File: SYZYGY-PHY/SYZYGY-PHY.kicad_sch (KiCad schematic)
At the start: 43 parts, among them J1 QTH-020-01-X-D-DP-A, J2 ARJM11C7-502-KB-EW2, J3 Conn_01x10, U1 GPY111, U2 TXB0106RGY, U3 TXB0106RGY, Y1 Crystal_GND24

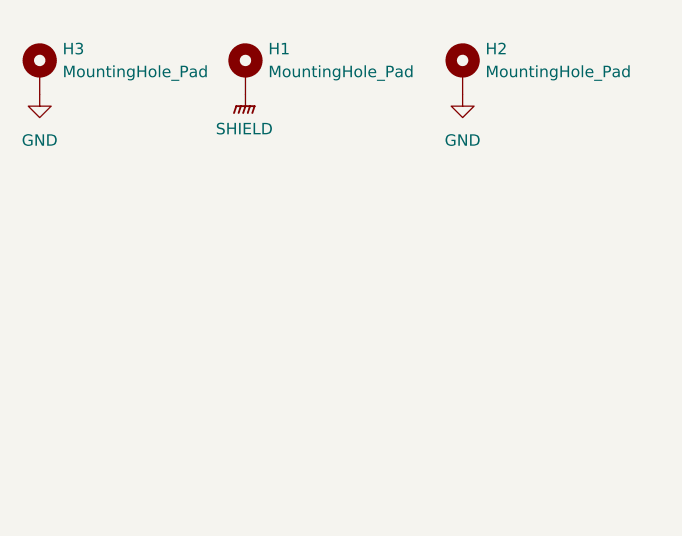
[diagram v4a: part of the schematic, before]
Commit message: adding power indicator LED
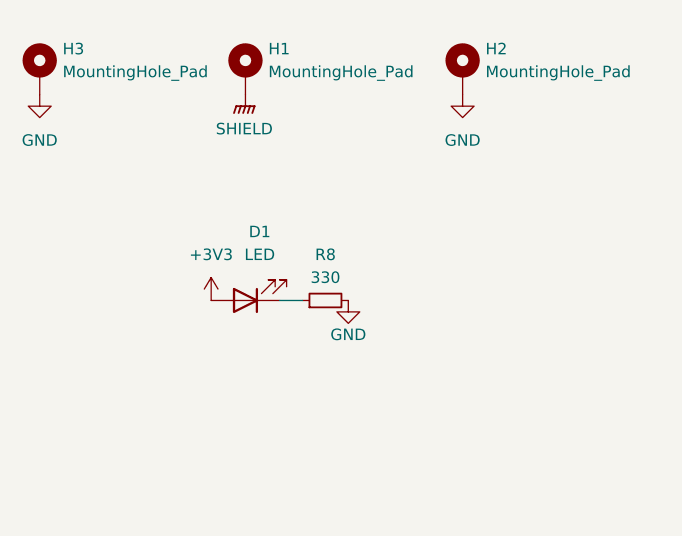
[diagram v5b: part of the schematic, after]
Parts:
- added D1: LED, LED_SMD:LED_0805_2012Metric, symbol Device:LED
- added R8: 330, Resistor_SMD:R_0805_2012Metric_Pad1.20x1.40mm_HandSolder, symbol Device:R_Small
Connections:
- net +3V3: now also D1.2 (A)
- net GND: now also R8.2
- new net: D1.1 (K), R8.1

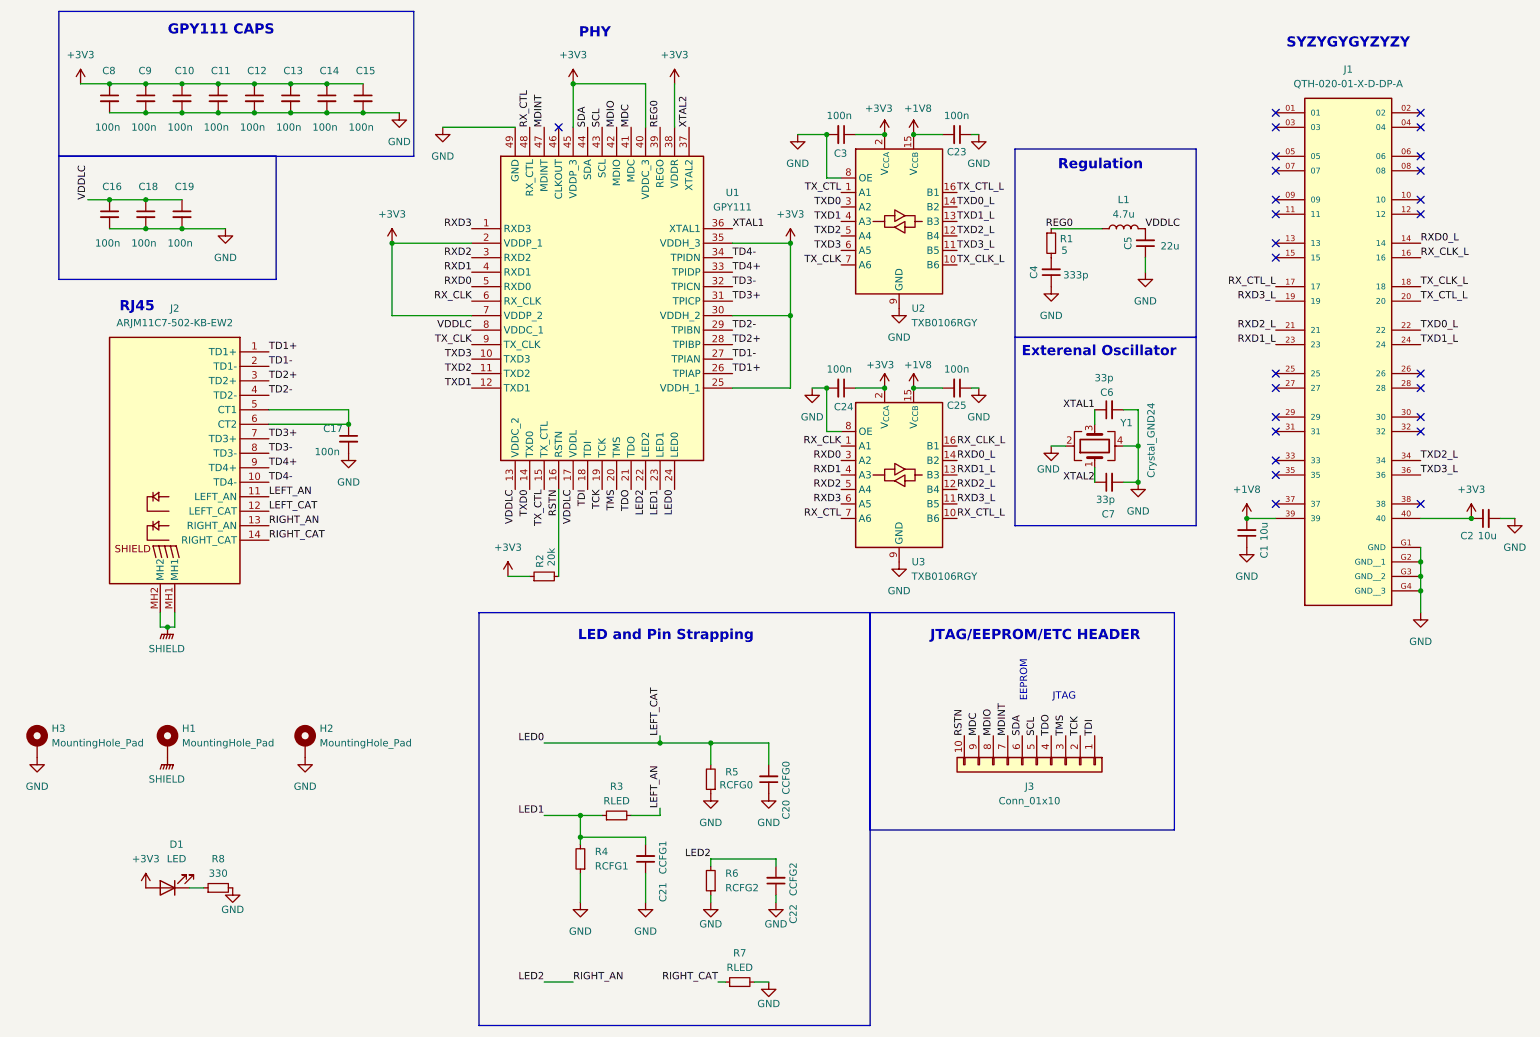
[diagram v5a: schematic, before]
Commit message: misc changes + SYZYGY-PHY fixes
fix up KiCad paths to be slightly friendlier to sharing between
machines; assert that we only want to use the library from `../`
relative so the 3d model path is valid.

SYZYGY-PHY fixes:
- add startup RC circuit to hold reset low for >1ms
- add calibration resistors between PHY C+/- and GND
- remove VDDLC from 3.3V net in schematic (not fully routed in PCB)
- update clock to a more frequency stable model, change CL caps accordingly
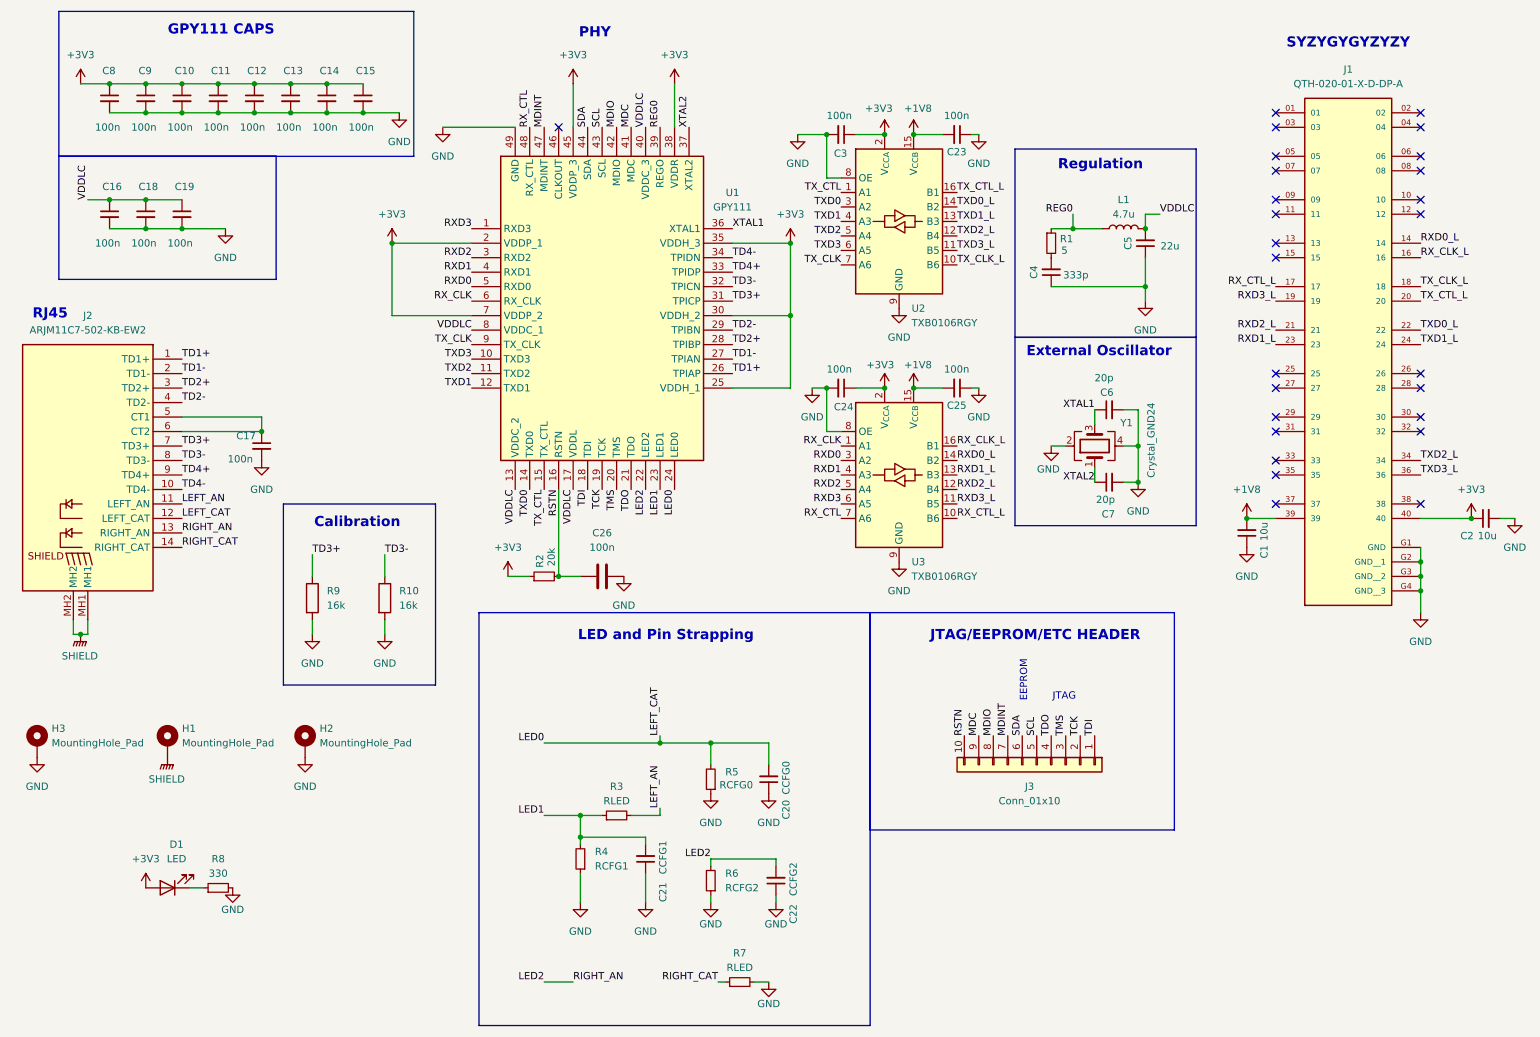
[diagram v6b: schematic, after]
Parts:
- added C26: 100n, Capacitor_SMD:C_0805_2012Metric_Pad1.18x1.45mm_HandSolder, symbol Device:C
- added R10, R9: 16k, Resistor_SMD:R_0805_2012Metric_Pad1.20x1.40mm_HandSolder, symbol Device:R
- C6, C7: value 33p -> 20p
- J2: App Note (none) -> https://ww1.microchip.com/downloads/en/Appnotes/VPPD-01740.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; Ref 2 (none) -> https://electronics.stackexchange.com/questions/637179/what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
- Y1: Manufacturer (none) -> TSX-3225 25.0000MF18X-G0; Mouser FA-238 25.0000MB-I -> 732-TSX-322MF18X-G
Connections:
- net +3V3: no longer U1.40 (VDDC_3)
- net GND: now also C26.1, R10.2, R9.2
- net RSTN: now also C26.2
- net TD3+: now also R9.1
- net TD3-: now also R10.1
- net VDDLC: now also U1.40 (VDDC_3)
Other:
- note added: "Calibration"
- note added: "External Oscillator"
- note removed: "Exterenal Oscillator"
- moved on the sheet: C17, J2

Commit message: adding inductor footprint for 2016 metric sized inductor, and changed L1 footprint and added to the pcb, updated the schematic with the new inductor part and datasheet link
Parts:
- L1: footprint Inductor_SMD:L_0805_2012Metric_Pad1.05x1.20mm_HandSolder -> local:Inductor 0806 (2016 metric); Part MLZ2012N4R7LT000 -> MAKK2016T4R7M
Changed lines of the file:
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@@
 			)
 		)
-		(property "Footprint" "Inductor_SMD:L_0805_2012Metric_Pad1.05x1.20mm_HandSolder"
+		(property "Footprint" "local:Inductor 0806 (2016 metric)"
 			(at 213.36 52.07 0)
 			(effects
@@
 			)
 		)
-		(property "Datasheet" "https://product.tdk.com/system/files/dam/doc/product/inductor/inductor/smd/catalog/inductor_commercial_decoupling_mlz2012_en.pdf"
+		(property "Datasheet" "https://www.mouser.com/datasheet/2/396/wound10_e-1396630.pdf"
 			(at 213.36 52.07 0)
 			(effects
@@
 			)
 		)
-		(property "Part" "MLZ2012N4R7LT000 "
+		(property "Part" "MAKK2016T4R7M"
 			(at 213.36 52.07 90)
 			(effects

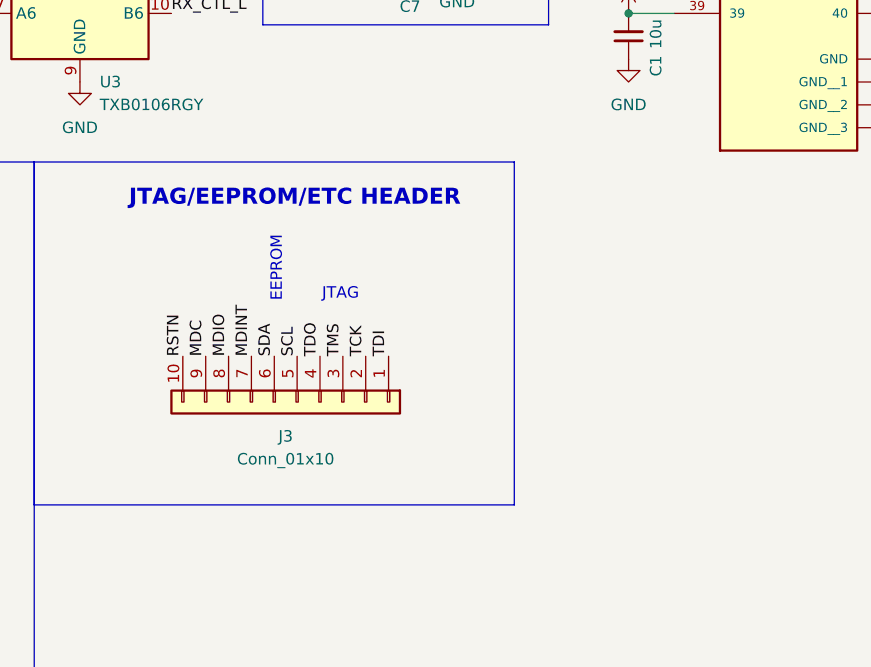
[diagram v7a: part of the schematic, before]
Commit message: adding a GND header, adding 3.3V and 1.8V 1x2 header
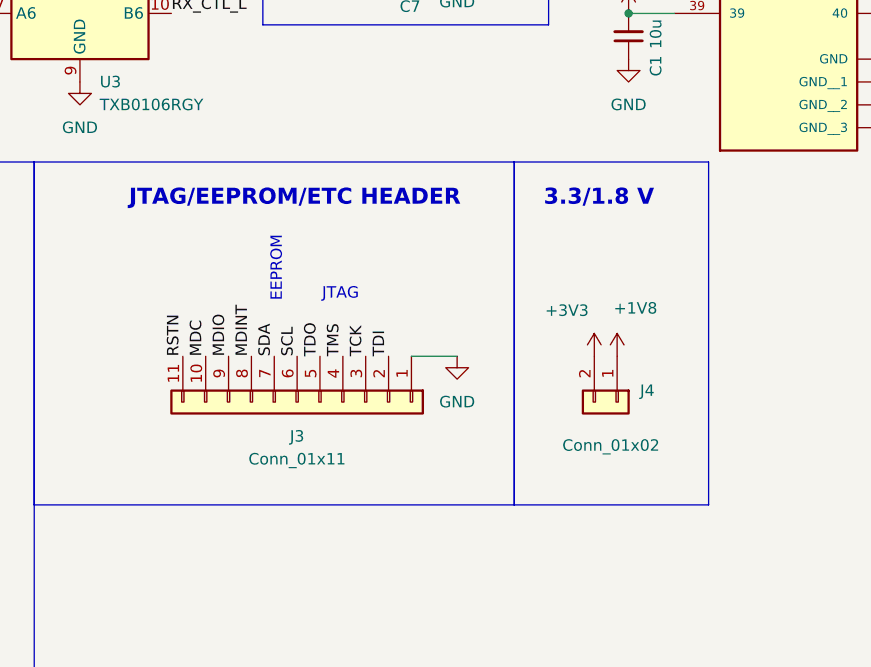
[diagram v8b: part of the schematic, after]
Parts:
- removed J3: Conn_01x10, Connector_PinSocket_2.54mm:PinSocket_1x10_P2.54mm_Vertical, symbol Connector_Generic:Conn_01x10
- added J3: Conn_01x11, Connector_PinSocket_2.54mm:PinSocket_1x11_P2.54mm_Vertical, symbol Connector_Generic:Conn_01x11
- added J4: Conn_01x02, Connector_PinHeader_2.54mm:PinHeader_1x02_P2.54mm_Vertical, symbol Connector_Generic:Conn_01x02
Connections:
- net +1V8: now also J4.1 (Pin_1)
- net +3V3: now also J4.2 (Pin_2)
- net GND: now also J3.1 (Pin_1)
- net MDC: now also J3.10 (Pin_10)
- net MDINT: now also J3.8 (Pin_8)
- net MDIO: now also J3.9 (Pin_9)
- net RSTN: now also J3.11 (Pin_11)
- net SCL: now also J3.6 (Pin_6)
- net SDA: now also J3.7 (Pin_7)
- net TCK: now also J3.3 (Pin_3)
- net TDI: now also J3.2 (Pin_2)
- net TDO: now also J3.5 (Pin_5)
- net TMS: now also J3.4 (Pin_4)
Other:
- note added: "3.3/1.8 V"
